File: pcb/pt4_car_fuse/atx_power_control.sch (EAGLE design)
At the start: 61 parts, among them IC2 REG1117, IC3 STM32F042F4, IC4 MY_7905DT, J1 ATX24RH, SW1 324_SW, SW2 324_SW, SW3 324_SW, SW4 324_SW, SW5 324_SW, SW7 324_SW, U1 USBC_16P, U2 USBC_16P

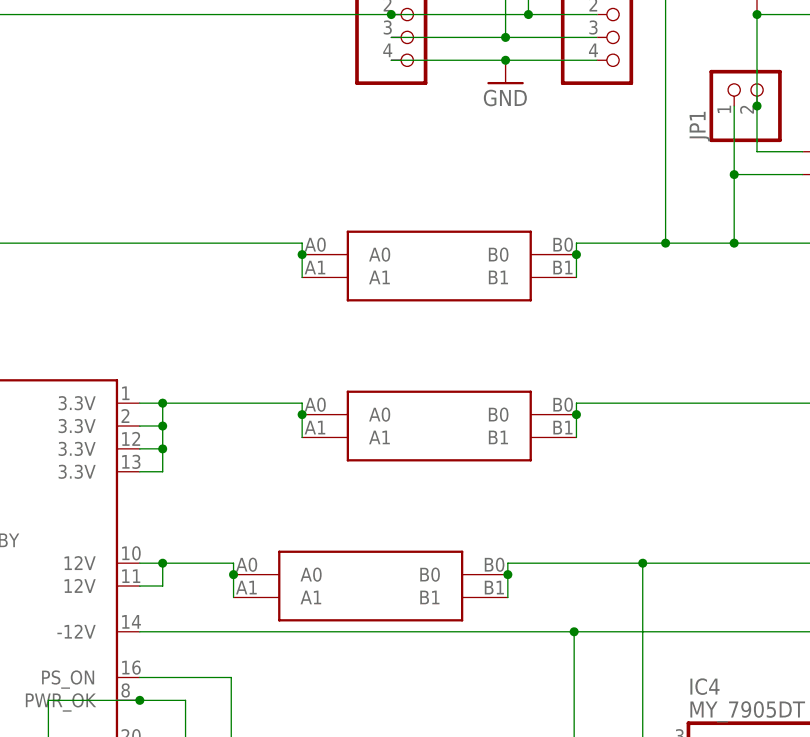
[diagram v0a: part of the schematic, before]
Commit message: fixed fuse holder footprint
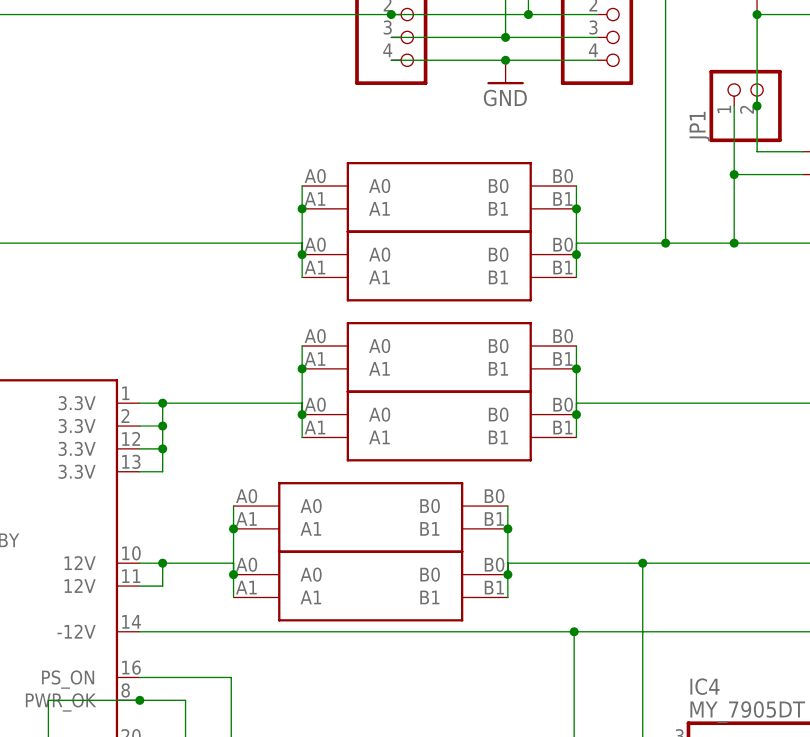
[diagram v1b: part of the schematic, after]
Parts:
- added U$4, U$6, U$9: FUSE_HOLDER, atx_power_control:FUSE_HOLDER
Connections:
- net N$10: now also U$9.A0, U$9.A1
- net N$14: now also U$6.A0, U$6.A1
- net N$15: now also U$4.B0, U$4.B1
- net N$16: now also U$6.B0, U$6.B1
- net N$21: now also U$4.A0, U$4.A1
- net N$30: now also U$9.B0, U$9.B1
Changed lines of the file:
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@@
 <part name="GND33" library="backplane" deviceset="GND" device=""/>
 <part name="R13" library="SparkFun-Passives" deviceset="RESISTOR" device="0805-RES" value="1K"/>
+<part name="U$4" library="atx_power_control" deviceset="FUSE_HOLDER" device=""/>
 <part name="U$5" library="atx_power_control" deviceset="CAR_FUSE_HOLDER" device="3IN1"/>
+<part name="U$6" library="atx_power_control" deviceset="FUSE_HOLDER" device=""/>
 <part name="U$7" library="atx_power_control" deviceset="CAR_FUSE_HOLDER" device="3IN1"/>
 <part name="U$8" library="atx_power_control" deviceset="CAR_FUSE_HOLDER" device="3IN1"/>
+<part name="U$9" library="atx_power_control" deviceset="FUSE_HOLDER" device=""/>
 <part name="JP4" library="pinhead" library_urn="urn:adsk.eagle:library:325" deviceset="PINHD-1X4" device="" package3d_urn="urn:adsk.eagle:package:22407/2"/>
 <part name="JP12" library="adafruit_changed" deviceset="PINHD-1X6" device=""/>
@@
 <attribute name="VALUE" x="394.97" y="36.322" size="1.778" layer="96" rot="R180"/>
 </instance>
+<instance part="U$4" gate="G$1" x="274.32" y="10.16" smashed="yes"/>
 <instance part="U$5" gate="G$1" x="274.32" y="2.54" smashed="yes"/>
+<instance part="U$6" gate="G$1" x="281.94" y="27.94" smashed="yes"/>
 <instance part="U$7" gate="G$1" x="281.94" y="20.32" smashed="yes"/>
 <instance part="U$8" gate="G$1" x="281.94" y="38.1" smashed="yes"/>
+<instance part="U$9" gate="G$1" x="281.94" y="45.72" smashed="yes"/>
 <instance part="JP4" gate="A" x="200.66" y="-71.12" smashed="yes">
 <attribute name="NAME" x="194.31" y="-62.865" size="1.778" layer="95"/>
@@
 <wire x1="266.954" y1="39.37" x2="266.954" y2="36.83" width="0.1524" layer="91"/>
 <junction x="266.954" y="39.37"/>
+<pinref part="U$9" gate="G$1" pin="A1"/>
+<wire x1="266.954" y1="39.37" x2="266.954" y2="44.45" width="0.1524" layer="91"/>
+<pinref part="U$9" gate="G$1" pin="A0"/>
+<wire x1="266.954" y1="44.45" x2="266.954" y2="46.99" width="0.1524" layer="91"/>
+<junction x="266.954" y="44.45"/>
 </segment>
 </net>
@@
 <wire x1="259.334" y1="3.81" x2="259.334" y2="1.27" width="0.1524" layer="91"/>
 <junction x="259.334" y="3.81"/>
+<pinref part="U$4" gate="G$1" pin="A1"/>
+<wire x1="259.334" y1="8.89" x2="259.334" y2="3.81" width="0.1524" layer="91"/>
+<pinref part="U$4" gate="G$1" pin="A0"/>
+<wire x1="259.334" y1="11.43" x2="259.334" y2="8.89" width="0.1524" layer="91"/>
+<junction x="259.334" y="8.89"/>
 </segment>
 </net>
@@
 <wire x1="266.954" y1="21.59" x2="266.954" y2="19.05" width="0.1524" layer="91"/>
 <junction x="266.954" y="21.59"/>
+<pinref part="U$6" gate="G$1" pin="A1"/>
+<wire x1="266.954" y1="21.59" x2="266.954" y2="26.67" width="0.1524" layer="91"/>
+<pinref part="U$6" gate="G$1" pin="A0"/>
+<wire x1="266.954" y1="26.67" x2="266.954" y2="29.21" width="0.1524" layer="91"/>
+<junction x="266.954" y="26.67"/>
 </segment>
 </net>
@@
 <wire x1="297.434" y1="39.37" x2="297.434" y2="36.83" width="0.1524" layer="91"/>
 <junction x="297.434" y="39.37"/>
+<pinref part="U$9" gate="G$1" pin="B1"/>
+<wire x1="297.434" y1="39.37" x2="297.434" y2="44.45" width="0.1524" layer="91"/>
+<pinref part="U$9" gate="G$1" pin="B0"/>
+<wire x1="297.434" y1="44.45" x2="297.434" y2="46.99" width="0.1524" layer="91"/>
+<junction x="297.434" y="44.45"/>
 <pinref part="JP12" gate="A" pin="1"/>
 <wire x1="276.86" y1="68.58" x2="299.72" y2="68.58" width="0.1524" layer="91"/>
@@
 <net name="N$15" class="0">
 <segment>
+<pinref part="U$4" gate="G$1" pin="B0"/>
+<pinref part="U$4" gate="G$1" pin="B1"/>
+<wire x1="289.814" y1="11.43" x2="289.814" y2="8.89" width="0.1524" layer="91"/>
 <pinref part="LED5" gate="G$1" pin="A"/>
 <wire x1="304.8" y1="5.08" x2="342.9" y2="5.08" width="0.1524" layer="91"/>
@@
 <wire x1="289.814" y1="5.08" x2="289.814" y2="3.81" width="0.1524" layer="91"/>
 <junction x="289.814" y="3.81"/>
+<wire x1="289.814" y1="8.89" x2="289.814" y2="3.81" width="0.1524" layer="91"/>
+<junction x="289.814" y="8.89"/>
 <pinref part="JP4" gate="A" pin="3"/>
 <junction x="198.12" y="-71.12"/>
@@
 <net name="N$16" class="0">
 <segment>
+<pinref part="U$6" gate="G$1" pin="B0"/>
+<pinref part="U$6" gate="G$1" pin="B1"/>
+<wire x1="297.434" y1="29.21" x2="297.434" y2="26.67" width="0.1524" layer="91"/>
 <pinref part="LED6" gate="G$1" pin="A"/>
 <wire x1="368.3" y1="25.4" x2="373.38" y2="25.4" width="0.1524" layer="91"/>
@@
 <wire x1="297.434" y1="21.59" x2="297.434" y2="19.05" width="0.1524" layer="91"/>
 <junction x="297.434" y="21.59"/>
-</segment>
-</net>
+<wire x1="297.434" y1="26.67" x2="297.434" y2="21.59" width="0.1524" layer="91"/>
+<junction x="297.434" y="26.67"/>
+</segment>
+</net>
